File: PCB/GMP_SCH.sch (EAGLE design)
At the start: 25 parts, among them CN1 1X4-3.5MM, CN2 1X4-3.5MM, IC1 MS560702BA03-50, J1 USB3075-30-A, Q1 TSM200N03DPQ33_RGG

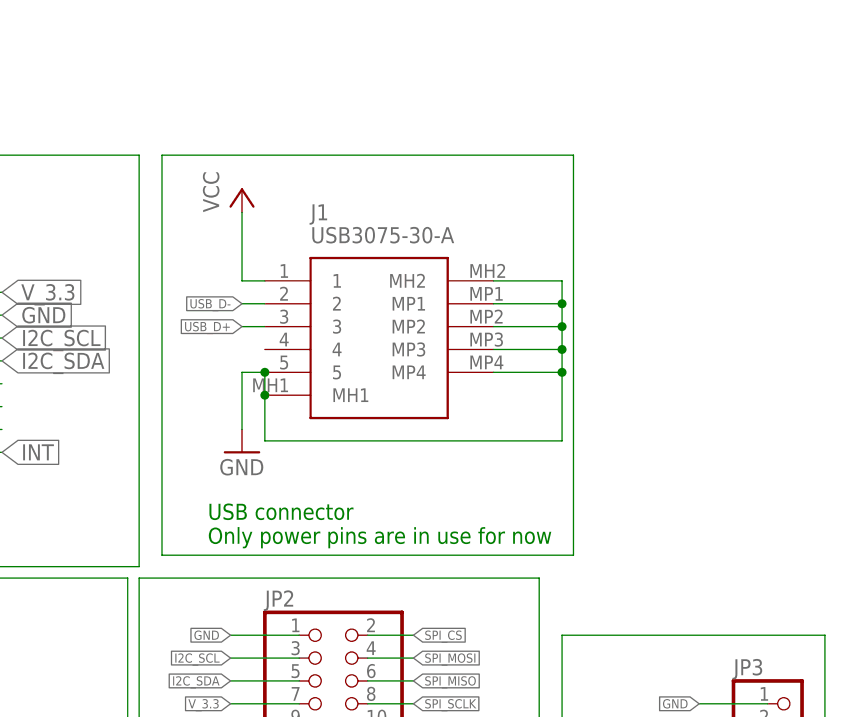
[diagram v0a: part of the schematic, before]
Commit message: Add files via upload
Update with routing and no usb connector anymore
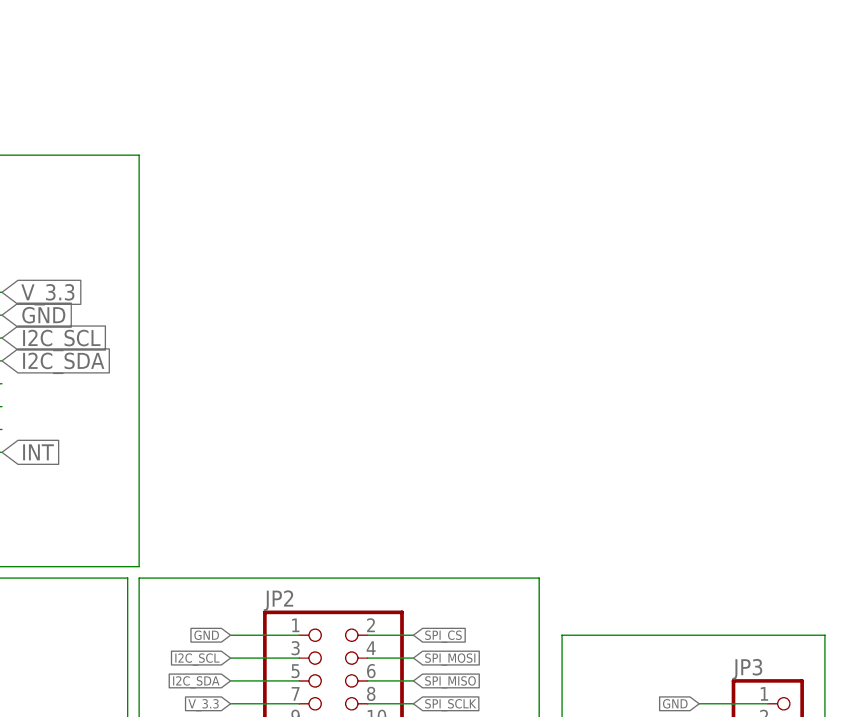
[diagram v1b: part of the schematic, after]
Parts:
- removed J1: USB3075-30-A, USB3075-30-A:USB3075-30-A
- R1, R12, R13, R14, R15, R16, R7, R8, R9: device rcl:R-US_R0805 -> adafruit:FLIPFLOP-RES
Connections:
- removed net USB_D+: J1.3
- removed net USB_D-: J1.2
- net GND: no longer J1.5, J1.MH1, J1.MH2, J1.MP1, J1.MP2, J1.MP3, J1.MP4
- net VCC: no longer J1.1
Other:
- note removed: "USB connector Only power pins are in use for now"
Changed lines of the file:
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@@
 <parts>
 <part name="IC1" library="MS560702BA03-50" deviceset="MS560702BA03-50" device=""/>
-<part name="J1" library="USB3075-30-A" deviceset="USB3075-30-A" device=""/>
-<part name="P+1" library="supply1" library_urn="urn:adsk.eagle:library:371" deviceset="VCC" device=""/>
-<part name="GND1" library="supply1" library_urn="urn:adsk.eagle:library:371" deviceset="GND" device=""/>
 <part name="C4" library="rcl" library_urn="urn:adsk.eagle:library:334" deviceset="C-US" device="C0805" package3d_urn="urn:adsk.eagle:package:23617/2" value="1u"/>
 <part name="C5" library="rcl" library_urn="urn:adsk.eagle:library:334" deviceset="C-US" device="C0805" package3d_urn="urn:adsk.eagle:package:23617/2" value="1u"/>
@@
 <part name="GND7" library="supply1" library_urn="urn:adsk.eagle:library:371" deviceset="GND" device=""/>
 <part name="C1" library="rcl" library_urn="urn:adsk.eagle:library:334" deviceset="C-US" device="C0805" package3d_urn="urn:adsk.eagle:package:23617/2" value="100n"/>
-<part name="R1" library="rcl" library_urn="urn:adsk.eagle:library:334" deviceset="R-US_" device="R0805" package3d_urn="urn:adsk.eagle:package:23553/2" value="10k"/>
-<part name="R7" library="rcl" library_urn="urn:adsk.eagle:library:334" deviceset="R-US_" device="R0805" package3d_urn="urn:adsk.eagle:package:23553/2" value="10k"/>
+<part name="R1" library="adafruit" deviceset="FLIPFLOP-RES" device="" value="10k"/>
+<part name="R7" library="adafruit" deviceset="FLIPFLOP-RES" device="" value="10k"/>
 <part name="GND9" library="supply1" library_urn="urn:adsk.eagle:library:371" deviceset="GND" device=""/>
 <part name="GND10" library="supply1" library_urn="urn:adsk.eagle:library:371" deviceset="GND" device=""/>
 <part name="S1" library="switch-omron" library_urn="urn:adsk.eagle:library:377" deviceset="10-XX" device="" package3d_urn="urn:adsk.eagle:package:27496/1"/>
-<part name="R8" library="rcl" library_urn="urn:adsk.eagle:library:334" deviceset="R-US_" device="R0805" package3d_urn="urn:adsk.eagle:package:23553/2" value="10k"/>
-<part name="R9" library="rcl" library_urn="urn:adsk.eagle:library:334" deviceset="R-US_" device="R0805" package3d_urn="urn:adsk.eagle:package:23553/2" value="2k"/>
+<part name="R8" library="adafruit" deviceset="FLIPFLOP-RES" device="" value="10k"/>
+<part name="R9" library="adafruit" deviceset="FLIPFLOP-RES" device="" value="2k"/>
 <part name="JP2" library="pinhead" library_urn="urn:adsk.eagle:library:325" deviceset="PINHD-2X7" device="" package3d_urn="urn:adsk.eagle:package:22478/2"/>
 <part name="JP3" library="pinhead" library_urn="urn:adsk.eagle:library:325" deviceset="PINHD-1X4" device="/90" package3d_urn="urn:adsk.eagle:package:22404/2"/>
@@
 <part name="CN2" library="adafruit" deviceset="1X4" device="-3.5MM"/>
 <part name="GND12" library="supply1" library_urn="urn:adsk.eagle:library:371" deviceset="GND" device=""/>
-<part name="R12" library="rcl" library_urn="urn:adsk.eagle:library:334" deviceset="R-US_" device="R0805" package3d_urn="urn:adsk.eagle:package:23553/2" value="0"/>
+<part name="R12" library="adafruit" deviceset="FLIPFLOP-RES" device="" value="0"/>
 <part name="GND13" library="supply1" library_urn="urn:adsk.eagle:library:371" deviceset="GND" device=""/>
-<part name="R13" library="rcl" library_urn="urn:adsk.eagle:library:334" deviceset="R-US_" device="R0805" package3d_urn="urn:adsk.eagle:package:23553/2" value="100k"/>
-<part name="R14" library="rcl" library_urn="urn:adsk.eagle:library:334" deviceset="R-US_" device="R0805" package3d_urn="urn:adsk.eagle:package:23553/2" value="27k"/>
-<part name="R15" library="rcl" library_urn="urn:adsk.eagle:library:334" deviceset="R-US_" device="R0805" package3d_urn="urn:adsk.eagle:package:23553/2" value="100k"/>
-<part name="R16" library="rcl" library_urn="urn:adsk.eagle:library:334" deviceset="R-US_" device="R0805" package3d_urn="urn:adsk.eagle:package:23553/2" value="27k"/>
+<part name="R13" library="adafruit" deviceset="FLIPFLOP-RES" device="" value="100k"/>
+<part name="R14" library="adafruit" deviceset="FLIPFLOP-RES" device="" value="27k"/>
+<part name="R15" library="adafruit" deviceset="FLIPFLOP-RES" device="" value="100k"/>
+<part name="R16" library="adafruit" deviceset="FLIPFLOP-RES" device="" value="27k"/>
 <part name="LS1" library="CMI-9605-0580T" deviceset="CMI-9605-0580T" device=""/>
 <part name="GND14" library="supply1" library_urn="urn:adsk.eagle:library:371" deviceset="GND" device=""/>
@@
 <text x="-83.82" y="146.05" size="1.778" layer="91">Pressure - Sensor</text>
 <text x="-81.28" y="182.88" size="1.778" layer="91">Enable pin needs connecting </text>
-<text x="15.24" y="147.32" size="1.778" layer="91">USB connector
-Only power pins are in use for now</text>
 <text x="-110.49" y="182.88" size="1.778" layer="91">3.3 V LDO</text>
 <text x="8.89" y="115.57" size="1.4224" layer="91">Data Bus</text>
@@
 <attribute name="VALUE" x="-86.36" y="168.91" size="1.778" layer="96" align="center-left"/>
 </instance>
-<instance part="J1" gate="G$1" x="21.59" y="176.53" smashed="yes">
-<attribute name="NAME" x="26.67" y="184.15" size="1.778" layer="95" align="center-left"/>
-<attribute name="VALUE" x="26.67" y="181.61" size="1.778" layer="96" align="center-left"/>
-</instance>
-<instance part="P+1" gate="VCC" x="19.05" y="186.69" smashed="yes">
-<attribute name="VALUE" x="16.51" y="184.15" size="1.778" layer="96" rot="R90"/>
-</instance>
-<instance part="GND1" gate="1" x="19.05" y="157.48" smashed="yes">
-<attribute name="VALUE" x="16.51" y="154.94" size="1.778" layer="96"/>
-</instance>
 <instance part="C4" gate="G$1" x="-96.52" y="196.85" smashed="yes">
 <attribute name="NAME" x="-95.504" y="197.485" size="1.778" layer="95"/>
@@
 <net name="VCC" class="0">
 <segment>
-<pinref part="J1" gate="G$1" pin="1"/>
-<pinref part="P+1" gate="VCC" pin="VCC"/>
-<wire x1="21.59" y1="176.53" x2="19.05" y2="176.53" width="0.1524" layer="91"/>
-<wire x1="19.05" y1="176.53" x2="19.05" y2="184.15" width="0.1524" layer="91"/>
-</segment>
-<segment>
 <pinref part="JP3" gate="A" pin="4"/>
 <wire x1="77.47" y1="121.92" x2="69.85" y2="121.92" width="0.1524" layer="91"/>
@@
 </net>
 <net name="GND" class="0">
-<segment>
-<pinref part="J1" gate="G$1" pin="5"/>
-<pinref part="GND1" gate="1" pin="GND"/>
-<wire x1="21.59" y1="166.37" x2="19.05" y2="166.37" width="0.1524" layer="91"/>
-<wire x1="19.05" y1="166.37" x2="19.05" y2="160.02" width="0.1524" layer="91"/>
-<pinref part="J1" gate="G$1" pin="MH1"/>
-<wire x1="21.59" y1="163.83" x2="21.59" y2="166.37" width="0.1524" layer="91"/>
-<junction x="21.59" y="166.37"/>
-<wire x1="21.59" y1="163.83" x2="21.59" y2="158.75" width="0.1524" layer="91"/>
-<junction x="21.59" y="163.83"/>
-<pinref part="J1" gate="G$1" pin="MH2"/>
-<wire x1="46.99" y1="176.53" x2="54.61" y2="176.53" width="0.1524" layer="91"/>
-<wire x1="54.61" y1="176.53" x2="54.61" y2="173.99" width="0.1524" layer="91"/>
-<pinref part="J1" gate="G$1" pin="MP4"/>
-<wire x1="54.61" y1="173.99" x2="54.61" y2="171.45" width="0.1524" layer="91"/>
-<wire x1="54.61" y1="171.45" x2="54.61" y2="168.91" width="0.1524" layer="91"/>
-<wire x1="54.61" y1="168.91" x2="54.61" y2="166.37" width="0.1524" layer="91"/>
-<wire x1="54.61" y1="166.37" x2="46.99" y2="166.37" width="0.1524" layer="91"/>
-<pinref part="J1" gate="G$1" pin="MP3"/>
-<wire x1="46.99" y1="168.91" x2="54.61" y2="168.91" width="0.1524" layer="91"/>
-<junction x="54.61" y="168.91"/>
-<pinref part="J1" gate="G$1" pin="MP2"/>
-<wire x1="46.99" y1="171.45" x2="54.61" y2="171.45" width="0.1524" layer="91"/>
-<junction x="54.61" y="171.45"/>
-<pinref part="J1" gate="G$1" pin="MP1"/>
-<wire x1="46.99" y1="173.99" x2="54.61" y2="173.99" width="0.1524" layer="91"/>
-<junction x="54.61" y="173.99"/>
-<wire x1="21.59" y1="158.75" x2="54.61" y2="158.75" width="0.1524" layer="91"/>
-<wire x1="54.61" y1="158.75" x2="54.61" y2="166.37" width="0.1524" layer="91"/>
-<junction x="54.61" y="166.37"/>
-</segment>
 <segment>
 <wire x1="-86.36" y1="196.85" x2="-88.9" y2="196.85" width="0.1524" layer="91"/>
@@
 </segment>
 </net>
-<net name="N$4" class="0">
-<segment>
-<wire x1="10.16" y1="190.5" x2="55.88" y2="190.5" width="0.1524" layer="91"/>
-<wire x1="55.88" y1="190.5" x2="55.88" y2="146.05" width="0.1524" layer="91"/>
-<wire x1="10.16" y1="190.5" x2="10.16" y2="146.05" width="0.1524" layer="91"/>
-<wire x1="10.16" y1="146.05" x2="55.88" y2="146.05" width="0.1524" layer="91"/>
-</segment>
-</net>
 <net name="N$6" class="0">
 <segment>
@@
 <wire x1="-101.6" y1="99.06" x2="-114.3" y2="99.06" width="0.1524" layer="91"/>
 <label x="-114.3" y="99.06" size="1.016" layer="95" rot="MR0" xref="yes"/>
-</segment>
-</net>
-<net name="USB_D-" class="0">
-<segment>
-<pinref part="J1" gate="G$1" pin="2"/>
-<wire x1="21.59" y1="173.99" x2="19.05" y2="173.99" width="0.1524" layer="91"/>
-<label x="19.05" y="173.99" size="1.016" layer="95" rot="R180" xref="yes"/>
-</segment>
-</net>
-<net name="USB_D+" class="0">
-<segment>
-<pinref part="J1" gate="G$1" pin="3"/>
-<wire x1="21.59" y1="171.45" x2="19.05" y2="171.45" width="0.1524" layer="91"/>
-<label x="19.05" y="171.45" size="1.016" layer="95" rot="R180" xref="yes"/>
 </segment>
 </net>
@@
 </drawing>
 <compatibility>
-<note version="6.3" minversion="6.2.2" severity="warning">
-Since Version 6.2.2 text objects can contain more than one line,
-which will not be processed correctly with this version.
-</note>
 <note version="8.2" severity="warning">
 Since Version 8.2, EAGLE supports online libraries. The ids

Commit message: rerouted the main board. one pin pending
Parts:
- R14: device adafruit:FLIPFLOP-RES -> rcl:R-EU_0207/12
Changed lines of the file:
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@@
 </variantdefs>
 <classes>
-<class number="0" name="default" width="0" drill="0">
-<clearance class="0" value="0.205"/>
+<class number="0" name="default" width="0.3048" drill="0">
+<clearance class="0" value="0.254"/>
 </class>
 </classes>
@@
 <part name="GND13" library="supply1" library_urn="urn:adsk.eagle:library:371" deviceset="GND" device=""/>
 <part name="R13" library="adafruit" deviceset="FLIPFLOP-RES" device="" value="100k"/>
-<part name="R14" library="adafruit" deviceset="FLIPFLOP-RES" device="" value="27k"/>
+<part name="R14" library="rcl" library_urn="urn:adsk.eagle:library:334" deviceset="R-EU_" device="0207/12" package3d_urn="urn:adsk.eagle:package:23489/1" value="27k"/>
 <part name="R15" library="adafruit" deviceset="FLIPFLOP-RES" device="" value="100k"/>
 <part name="R16" library="adafruit" deviceset="FLIPFLOP-RES" device="" value="27k"/>
@@
 packages will not be understood (or retained) with this version.
 </note>
+<note version="8.4" severity="warning">
+Since Version 8.4, EAGLE supports properties for SPICE simulation.
+Probes in schematics and SPICE mapping objects found in parts and library devices
+will not be understood with this version. Update EAGLE to the latest version
+for full support of SPICE simulation.
+</note>
 </compatibility>

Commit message: Add files via upload
Fixed silly little airwire due to decals
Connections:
- net INT: now also U$1.30-CRX3; no longer U$1.17-A3/TX4/SDA1
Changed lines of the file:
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@@
 </segment>
 <segment>
-<pinref part="U$1" gate="G$1" pin="17-A3/TX4/SDA1"/>
-<wire x1="-101.6" y1="109.22" x2="-106.68" y2="109.22" width="0.1524" layer="91"/>
-<label x="-106.68" y="109.22" size="1.778" layer="95" rot="R180" xref="yes"/>
+<pinref part="U$1" gate="G$1" pin="30-CRX3"/>
+<wire x1="-101.6" y1="68.58" x2="-109.22" y2="68.58" width="0.1524" layer="91"/>
+<label x="-109.22" y="68.58" size="1.778" layer="95" rot="R180" xref="yes"/>
 </segment>
 </net>
